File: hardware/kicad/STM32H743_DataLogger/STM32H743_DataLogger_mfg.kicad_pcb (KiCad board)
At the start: 4 copper layers, 160 x 100 mm, 172 parts, among them J1 24VDC_Input, J10 SWD_Debug, J11 USB-C, J12 UART_Debug, J13 BOOT0_Select, J14 TC2050-IDC, J20 AI_CH0, J21 AI_CH1, J22 AI_CH2, J23 AI_CH3, J30 DI_0, J31 DI_1, J32 DI_2, J33 DI_3, J34 DI_4, J35 DI_5, J36 DI_6, J37 DI_7, J40 DO_0, J41 DO_1, J42 DO_2, J43 DO_3, J50 RS485, J51 CAN, J60 J0011D21BNL, J70 SMA_LoRa, J71 U.FL_WiFi, J72 NanoSIM, J73 SMA_LTE, J74 SMA_GNSS, J80 microSD, K1 HF46F-G, Q1 SI4435DDY, U1 TPS54560, U10 STM32H743VIT6, U2 TLV1117LV33, U20 OPA2376, U3 TPS7A4533, U30 TLP293, U31 ULN2003A, U40 ISO3082, U41 ISO1042, U50 W5500, U60 SX1276, U61 ATWINC1500, U62 SIM7600G-H, U62B RN4870, U63 TPS73641, U64 TPS3823-33, U70 W25Q64JV, U71 AT24C256C, Y1 25MHz, Y2 32.768kHz, Y3 25MHz, Y4 32MHz

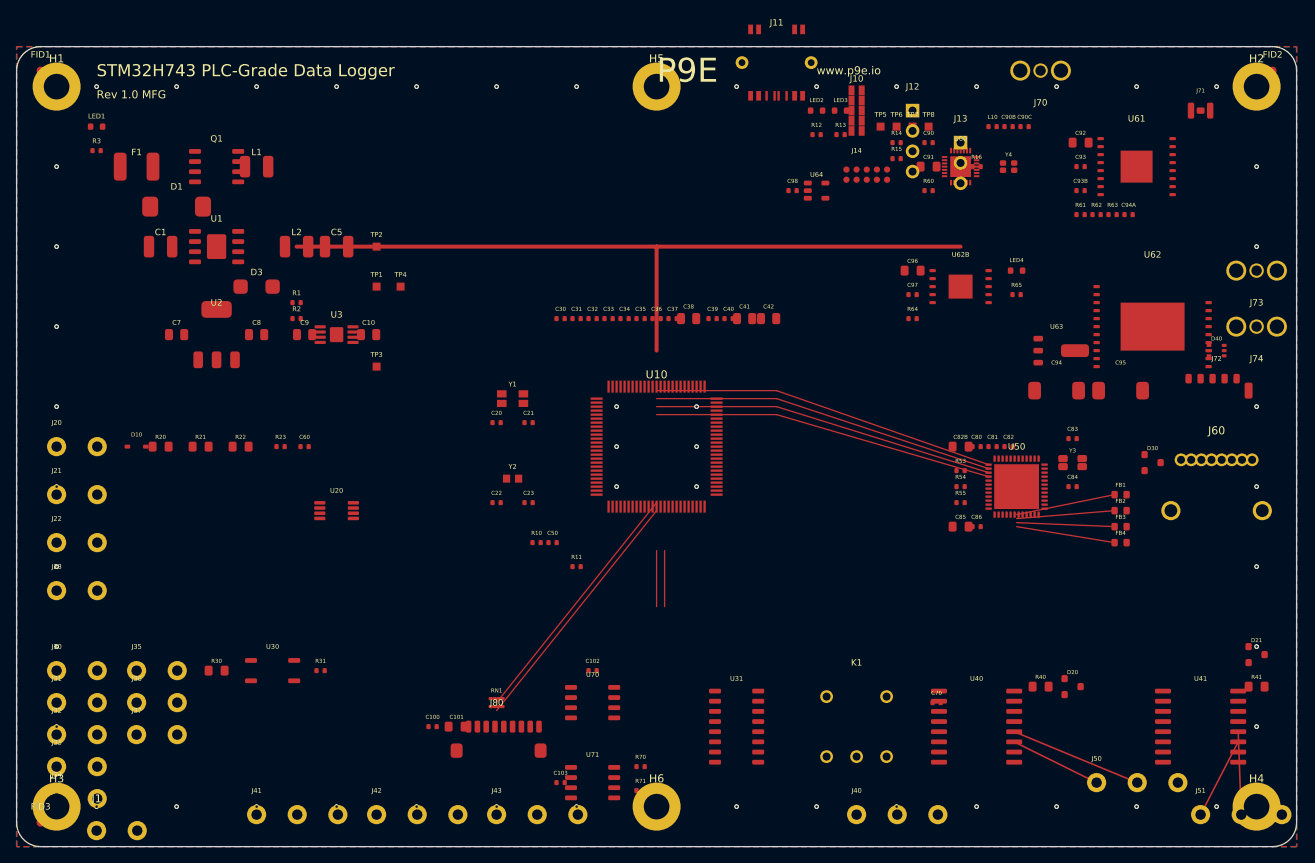
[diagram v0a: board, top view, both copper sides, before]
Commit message: Complete mfg PCB placement, fix designator conflicts, sync BOM
Manufacturing PCB (STM32H743_DataLogger_mfg.kicad_pcb):
- Add all missing multi-channel footprints: analog channels 1-3
  (D11-D13, R24-R35, C61-C63) plus second op-amp U21
- Add full 8-channel digital input chain (R100-R107 limiters,
  U30/U32-U38 optocouplers, R108-R115 pull-ups) with new
  DI_n_LED nets instead of floating net 0
- Add relays K2-K4 and replace the oversized SANYOU SRD placeholder
  with an HF46F-G/5-HS1T form-A footprint; wire relay contacts to
  J40-J43 via new DOn_NO / DOn_COM nets
- Add C104 (EEPROM decoupling), LED4 + R17 (comm activity indicator)
- Rename the BLE indicator from LED4 to LED5 to match the schematic
- Replace silkscreen branding with the full P9E block (company mark,
  P9E Microsystems Pvt Ltd, www.p9e.in, product, specs) on F.SilkS and
  P/N, S/N, compliance marks and origin on B.SilkS; www.p9e.io and the
  stale "SCADA Systems" text are gone
- Resolve all 26 footprint overlaps, pull the USB-C receptacle fully
  on-board, move fiducials clear of mounting holes, and drop the 22
  stitching vias that landed on pads

Schematics:
- Renumber Digital_IO resistors to R100-R115 and the eighth
  optocoupler to U38, removing the R31x/R40x placeholder designators
  and the R30/R31/R40/R41 collisions with Analog_Inputs and RS485_CAN
- Add C104 to Storage and LED4 + R17 to the MCU sheet

BOM: update the digital I/O and analog designator ranges to match,
add R17, correct the relay type to SPST-NO, and refresh the totals
(116 line items, 211 components).

Co-Authored-By: Claude Opus 5 <noreply@anthropic.com>
Claude-Session: https://claude.ai/code/session_01XsiZ6LJT6X46LKY8yEbRbx
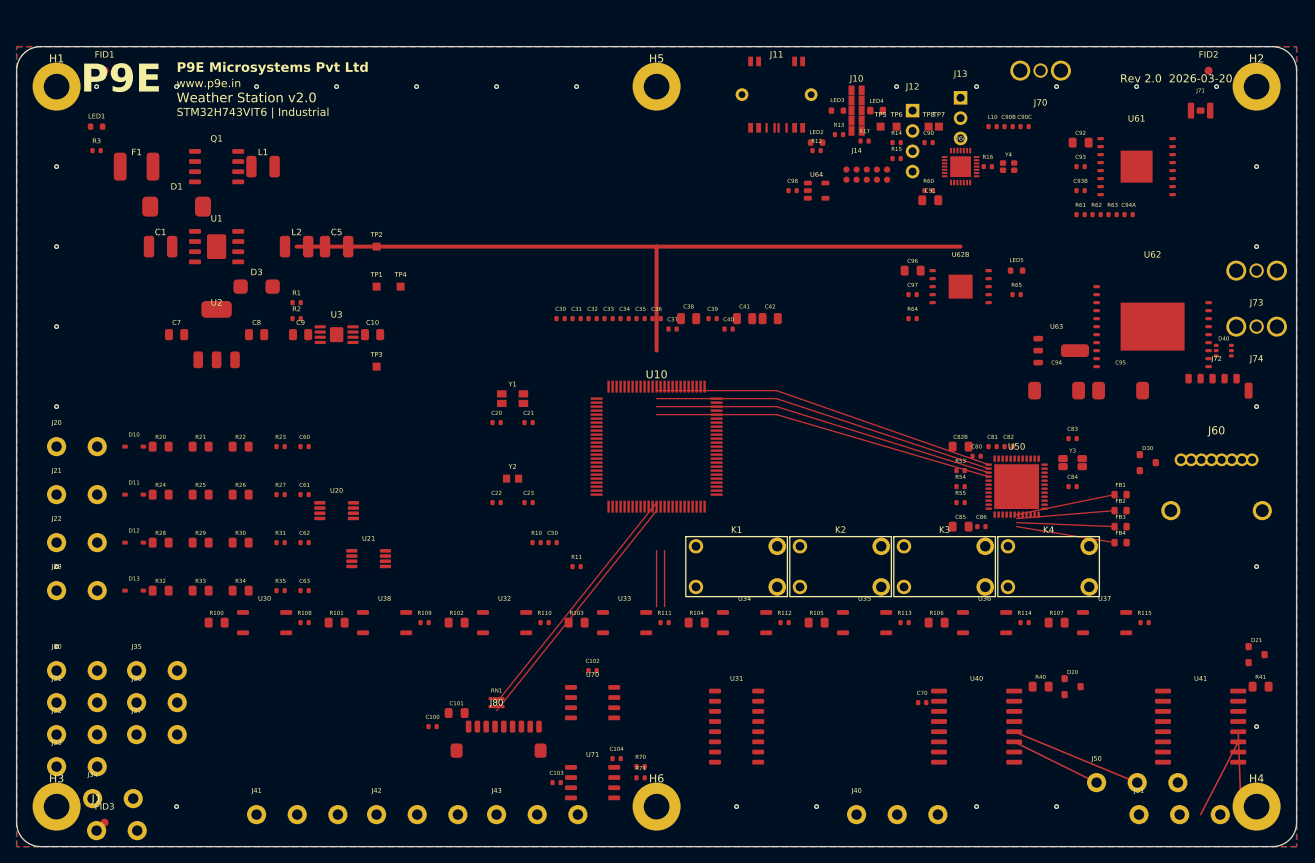
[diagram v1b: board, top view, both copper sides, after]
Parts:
- added C104: 100nF, Capacitor_SMD:C_0402_1005Metric, F.Cu at (75.0, 89.0)
- added C61: 100nF, Capacitor_SMD:C_0402_1005Metric, F.Cu at (36.0, 56.0)
- added C62: 100nF, Capacitor_SMD:C_0402_1005Metric, F.Cu at (36.0, 62.0)
- added C63: 100nF, Capacitor_SMD:C_0402_1005Metric, F.Cu at (36.0, 68.0)
- added D11: PESD5V0S1BA, Diode_SMD:D_SOD-323, F.Cu at (14.7, 56.0)
- added D12: PESD5V0S1BA, Diode_SMD:D_SOD-323, F.Cu at (14.7, 62.0)
- added D13: PESD5V0S1BA, Diode_SMD:D_SOD-323, F.Cu at (14.7, 68.0)
- added K2: HF46F-G/5-HS1T, Relay_THT:Relay_SPST_HF46F-G_Form_A, F.Cu at (103.0, 65.0)
- added K3: HF46F-G/5-HS1T, Relay_THT:Relay_SPST_HF46F-G_Form_A, F.Cu at (116.0, 65.0)
- added K4: HF46F-G/5-HS1T, Relay_THT:Relay_SPST_HF46F-G_Form_A, F.Cu at (129.0, 65.0)
- added LED5: Blue_BLE, LED_SMD:LED_0603_1608Metric, F.Cu at (125.0, 28.0)
- added R100: 4.7k, Resistor_SMD:R_0805_2012Metric, F.Cu at (25.0, 72.0)
- added R101: 4.7k, Resistor_SMD:R_0805_2012Metric, F.Cu at (40.0, 72.0)
- added R102: 4.7k, Resistor_SMD:R_0805_2012Metric, F.Cu at (55.0, 72.0)
- added R103: 4.7k, Resistor_SMD:R_0805_2012Metric, F.Cu at (70.0, 72.0)
- added R104: 4.7k, Resistor_SMD:R_0805_2012Metric, F.Cu at (85.0, 72.0)
- added R105: 4.7k, Resistor_SMD:R_0805_2012Metric, F.Cu at (100.0, 72.0)
- added R106: 4.7k, Resistor_SMD:R_0805_2012Metric, F.Cu at (115.0, 72.0)
- added R107: 4.7k, Resistor_SMD:R_0805_2012Metric, F.Cu at (130.0, 72.0)
- added R108: 10k, Resistor_SMD:R_0402_1005Metric, F.Cu at (36.0, 72.0)
- added R109: 10k, Resistor_SMD:R_0402_1005Metric, F.Cu at (51.0, 72.0)
- added R110: 10k, Resistor_SMD:R_0402_1005Metric, F.Cu at (66.0, 72.0)
- added R111: 10k, Resistor_SMD:R_0402_1005Metric, F.Cu at (81.0, 72.0)
- added R112: 10k, Resistor_SMD:R_0402_1005Metric, F.Cu at (96.0, 72.0)
- added R113: 10k, Resistor_SMD:R_0402_1005Metric, F.Cu at (111.0, 72.0)
- added R114: 10k, Resistor_SMD:R_0402_1005Metric, F.Cu at (126.0, 72.0)
- added R115: 10k, Resistor_SMD:R_0402_1005Metric, F.Cu at (141.0, 72.0)
- added R17: 1k, Resistor_SMD:R_0402_1005Metric, F.Cu at (106.0, 11.8)
- added R24: 249R, Resistor_SMD:R_0805_2012Metric, F.Cu at (18.0, 56.0)
- added R25: 20k, Resistor_SMD:R_0805_2012Metric, F.Cu at (23.0, 56.0)
- added R26: 10k, Resistor_SMD:R_0805_2012Metric, F.Cu at (28.0, 56.0)
- added R27: 1k, Resistor_SMD:R_0402_1005Metric, F.Cu at (33.0, 56.0)
- added R28: 249R, Resistor_SMD:R_0805_2012Metric, F.Cu at (18.0, 62.0)
- added R29: 20k, Resistor_SMD:R_0805_2012Metric, F.Cu at (23.0, 62.0)
- added R32: 249R, Resistor_SMD:R_0805_2012Metric, F.Cu at (18.0, 68.0)
- added R33: 20k, Resistor_SMD:R_0805_2012Metric, F.Cu at (23.0, 68.0)
- added R34: 10k, Resistor_SMD:R_0805_2012Metric, F.Cu at (28.0, 68.0)
- added R35: 1k, Resistor_SMD:R_0402_1005Metric, F.Cu at (33.0, 68.0)
- added U21: OPA2376, Package_SO:MSOP-8_3x3mm_P0.65mm, F.Cu at (44.0, 64.0)
- added U32: TLP293, Package_SO:SOP-4_3.8x4.1mm_P2.54mm, F.Cu at (61.0, 72.0)
- added U33: TLP293, Package_SO:SOP-4_3.8x4.1mm_P2.54mm, F.Cu at (76.0, 72.0)
- added U34: TLP293, Package_SO:SOP-4_3.8x4.1mm_P2.54mm, F.Cu at (91.0, 72.0)
- added U35: TLP293, Package_SO:SOP-4_3.8x4.1mm_P2.54mm, F.Cu at (106.0, 72.0)
- added U36: TLP293, Package_SO:SOP-4_3.8x4.1mm_P2.54mm, F.Cu at (121.0, 72.0)
- added U37: TLP293, Package_SO:SOP-4_3.8x4.1mm_P2.54mm, F.Cu at (136.0, 72.0)
- added U38: TLP293, Package_SO:SOP-4_3.8x4.1mm_P2.54mm, F.Cu at (46.0, 72.0)
- K1: value HF46F-G -> HF46F-G/5-HS1T; footprint Relay_THT:Relay_SPDT_SANYOU_SRD_Series_Form_C -> Relay_THT:Relay_SPST_HF46F-G_Form_A
- LED4: value Blue_BLE -> Orange COMM
- R30: value 4.7k -> 10k
- R31: value 10k -> 1k
- moved LED4 26.6 mm to (107.5, 8.00)
- moved K1 25.0 mm to (90.0, 65.0)
- moved R31 16.8 mm to (33.0, 62.0)
- moved R30 16.3 mm to (28.0, 62.0)
- moved FID1 8.00 mm to (11.0, 3.00)
- moved FID2 8.00 mm to (149.0, 3.00)
- moved FID3 8.00 mm to (11.0, 97.0)
- moved J51 7.70 mm to (140.3, 96.0)
- moved U30 6.08 mm to (31.0, 72.0)
- moved J13 5.60 mm to (118.0, 6.40)
- moved J34 4.50 mm to (9.50, 94.0)
- moved C91 4.20 mm to (114.2, 19.2)
- moved J11 4.00 mm to (95.0, 6.00)
- moved LED2 4.00 mm to (100.0, 12.0)
- moved TP7 3.30 mm to (115.3, 10.0)
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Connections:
- J40 pad 1: (no net) -> DO0_NO
- J40 pad 2: (no net) -> DO0_COM
- J41 pad 1: (no net) -> DO1_NO
- J41 pad 2: (no net) -> DO1_COM
- J42 pad 1: (no net) -> DO2_NO
- J42 pad 2: (no net) -> DO2_COM
- J43 pad 1: (no net) -> DO3_NO
- J43 pad 2: (no net) -> DO3_COM
- K1 pad 3: (no net) -> DO0_COM
- K1 pad 4: (no net) -> DO0_NO
- LED4 pad 1: BLE_STATUS -> LED_COMM
- LED4 pad 2: (no net) -> +3V3
- R30 pad 1: DI_0_ISO -> AI_CH2_FILT
- R30 pad 2: (no net) -> GND
- R31 pad 1: +3V3 -> AI_CH2_FILT
- R31 pad 2: DI_0 -> ADC1_CH2
- U30 pad 1: (no net) -> DI_0_LED
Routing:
- net GND: vias 48 -> 28
- net +3V3: vias 2 -> 0
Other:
- board text added: "24VDC 4-20mA x4 DI x8 DO x4"
- board text added: "CE RoHS WEEE"
- board text added: "ETH / LoRa / WiFi / BLE / LTE"
- board text added: "Made in India"
- board text added: "P/N: P9E-WS-200"
- board text added: "P9E Microsystems Pvt Ltd"
- board text added: "Rev 2.0 2026-03-20"
- board text added: "S/N: ________"
- board text added: "STM32H743VIT6 | Industrial"
- board text added: "Weather Station v2.0"
- board text added: "www.p9e.in"
- board text removed: "Rev 1.0 MFG"
- board text removed: "SCADA Systems"
- board text removed: "STM32H743 PLC-Grade Data Logger"
- board text removed: "www.p9e.io"

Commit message: Re-floorplan mfg PCB on real courtyards; make the isolation real
Footprints carried pads only, so collision checks were meaningless — a
10x9.6mm terminal block measured as 2.4mm. Every footprint now has an
F.CrtYd body rect (package body union pad extents), which exposed 74
courtyard collisions the old pad-only check called clean, including
terminal blocks stacked at 4mm pitch and the 30x30mm SIM7600 sitting on
top of six neighbours.

Placement is now generated by an explicit floorplan rather than nudged:
- Field wiring lives on the two long edges. Bottom: 24VDC in, the four
  analog inputs, then the four relay outputs. Top: RS485 and CAN behind
  the isolation barrier, then the eight digital inputs.
- RJ45, USB-C and the three SMA antennas moved to the right edge;
  microSD to the left.
- Each circuit block is packed into a region adjacent to its own
  connector (analog over its terminals, relays over theirs, W5500
  beside the RJ45, and so on), at 33-65% area fill.
- Result: 223 footprints, zero courtyard collisions, nothing off-board.

Two isolation defects found and fixed:
- ISO3082 and ISO1042 had no isolated bus-side supply at all —
  RS485_ISO_VCC and CAN_ISO_VCC were undriven, so the 5kVrms parts could
  not work. Added U42/U43 (NXJ1S0505MC-R13, 5.2kVDC 1W) and C71-C74.
- The optocoupled digital inputs were not isolated: every TLP293 LED
  cathode and every field terminal's second pin sat on logic GND, making
  the field wiring and logic ground one node. Added a floating DI_COM
  field return and moved both onto it.

Isolation is now built into the copper: the GND and +3V3 pours are
notched away from the top-left corner, the RS485 and CAN field sides get
their own floating pours (8mm to main copper on the outside, 4mm between
the two domains), milled slots run under U40-U43 where they cross the
barrier, and a copper keepout on all four layers stops any layer
bridging the optocoupler row. Verified: no logic-net pad lies inside the
isolated pocket. The isolato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
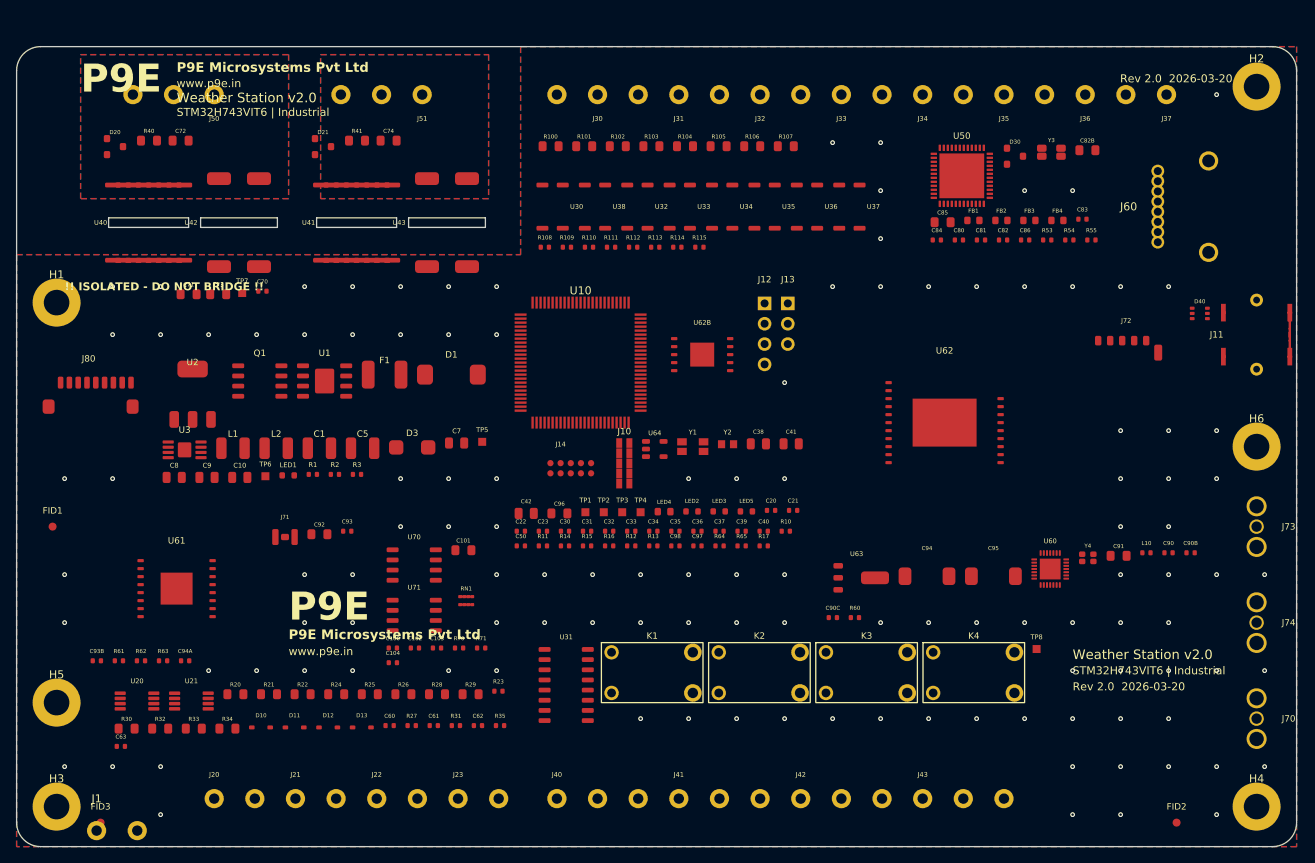
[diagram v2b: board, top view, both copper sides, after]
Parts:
- added C71: 10uF, Capacitor_SMD:C_0805_2012Metric, F.Cu at (21.5, 30.9)
- added C72: 10uF, Capacitor_SMD:C_0805_2012Metric, F.Cu at (20.5, 11.8)
- added C73: 10uF, Capacitor_SMD:C_0805_2012Metric, F.Cu at (25.2, 30.9)
- added C74: 10uF, Capacitor_SMD:C_0805_2012Metric, F.Cu at (46.5, 11.8)
- added U42: NXJ1S0505MC, Converter_DCDC:Converter_DCDC_NXJ1S_SMD, F.Cu at (27.8, 22.0)
- added U43: NXJ1S0505MC, Converter_DCDC:Converter_DCDC_NXJ1S_SMD, F.Cu at (53.8, 22.0)
- moved J37 151.6 mm to (143.7, 6.00), turned to 180 degrees
- moved J36 140.8 mm to (133.6, 6.00), turned to 180 degrees
- moved J50 139.9 mm to (24.7, 6.00), turned to 180 degrees
- moved D20 137.4 mm to (12.3, 12.5)
- moved C93B 136.3 mm to (10.0, 76.8)
- moved J34 136.1 mm to (113.3, 6.00), turned to 180 degrees
- moved D21 132.9 mm to (38.3, 12.5)
- moved R61 132.5 mm to (12.8, 76.8)
- moved R41 132.0 mm to (42.5, 11.8)
- moved R62 131.8 mm to (15.6, 76.8)
- moved R63 131.1 mm to (18.3, 76.8)
- moved U61 131.1 mm to (20.0, 67.8)
- moved R40 130.7 mm to (16.6, 11.8)
- moved C94A 130.5 mm to (21.1, 76.8)
- moved J35 130.1 mm to (123.4, 6.00), turned to 180 degrees
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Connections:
- J30 pad 2: GND -> DI_COM
- J31 pad 2: GND -> DI_COM
- J32 pad 2: GND -> DI_COM
- J33 pad 2: GND -> DI_COM
- J34 pad 2: GND -> DI_COM
- J35 pad 2: GND -> DI_COM
- J36 pad 2: GND -> DI_COM
- J37 pad 2: GND -> DI_COM
- U30 pad 2: GND -> DI_COM
- U32 pad 2: GND -> DI_COM
- U33 pad 2: GND -> DI_COM
- U34 pad 2: GND -> DI_COM
- U35 pad 2: GND -> DI_COM
- U36 pad 2: GND -> DI_COM
- U37 pad 2: GND -> DI_COM
- U38 pad 2: GND -> DI_COM
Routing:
- net +3V3: track 96.0 -> 0.00 mm
- net SPI4_SCK: track 43.1 -> 0.00 mm
- net SPI4_MISO: track 42.9 -> 0.00 mm
- net SPI4_MOSI: track 42.8 -> 0.00 mm
- net NSS_ETH: track 42.6 -> 0.00 mm
- net SDMMC1_D0: track 32.0 -> 0.00 mm
- net SDMMC1_CLK: track 32.0 -> 0.00 mm
- net RS485_B: track 16.6 -> 0.00 mm
- net ETH_TXP: track 12.5 -> 0.00 mm
- net ETH_RXN: track 12.4 -> 0.00 mm
- net ETH_TXN: track 12.3 -> 0.00 mm
- net ETH_RXP: track 12.3 -> 0.00 mm
- net RS485_A: track 11.5 -> 0.00 mm
- net CAN_L: track 10.4 -> 0.00 mm
- net CAN_H: track 10.2 -> 0.00 mm
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- added copper zone on B.Cu, net CAN_ISO_GND
- added copper zone on F.Cu, net CAN_ISO_GND
- added copper zone on B.Cu, net RS485_ISO_GND
- added copper zone on F.Cu, net RS485_ISO_GND
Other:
- outline, holes or cut-outs redrawn
- board text added: "!! ISOLATED - DO NOT BRIDGE !!"
- board text added: "24VDC in | 4-20mA x4 | DI x8 | DO x4"
- board text added: "4-layer FR-4 TG170 | ENIG | -40..+85C"
- board text added: "CE RoHS WEEE Made in India"
- board text added: "Do not bridge the slots under U40-U43"
- board text added: "ETH / LoRa / WiFi / BLE / LTE / GNSS"
- board text added: "RS485/CAN field side is galvanically isolated"
- board text added: "S/N: ____________"
